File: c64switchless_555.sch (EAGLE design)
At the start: 21 parts, among them IC1 7474N-RP, IC2 NE555, IC3 PIC12F629P, T1 BC547, T2 BC547, X1 B4B-ZR

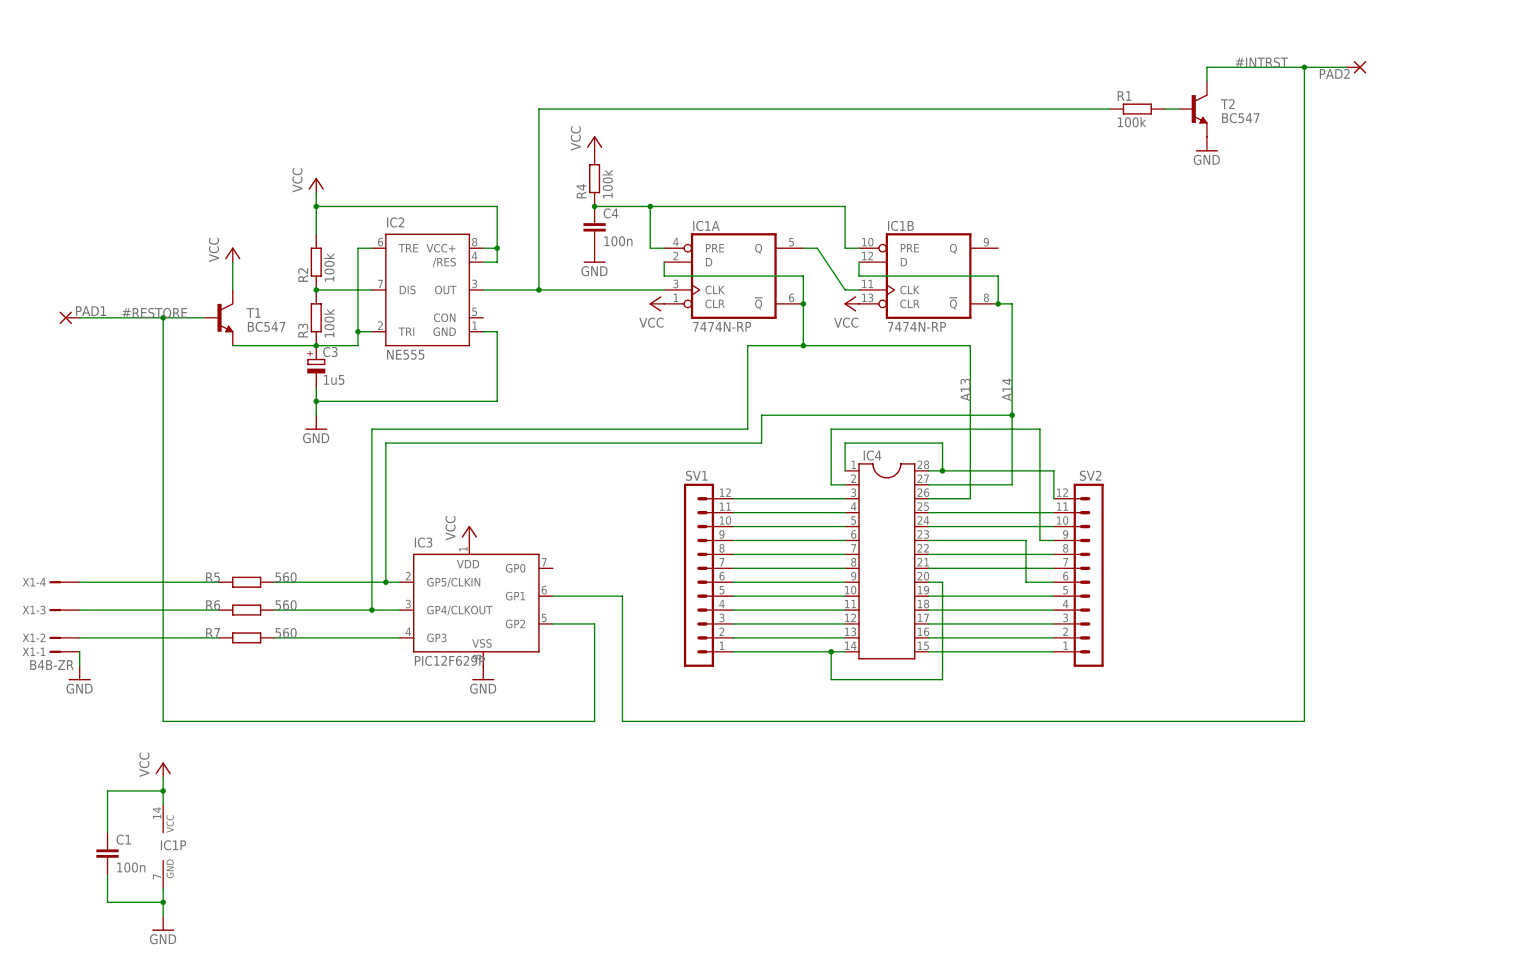
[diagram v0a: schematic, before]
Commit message: PDF file added
Note that this 555 based design is not completed.
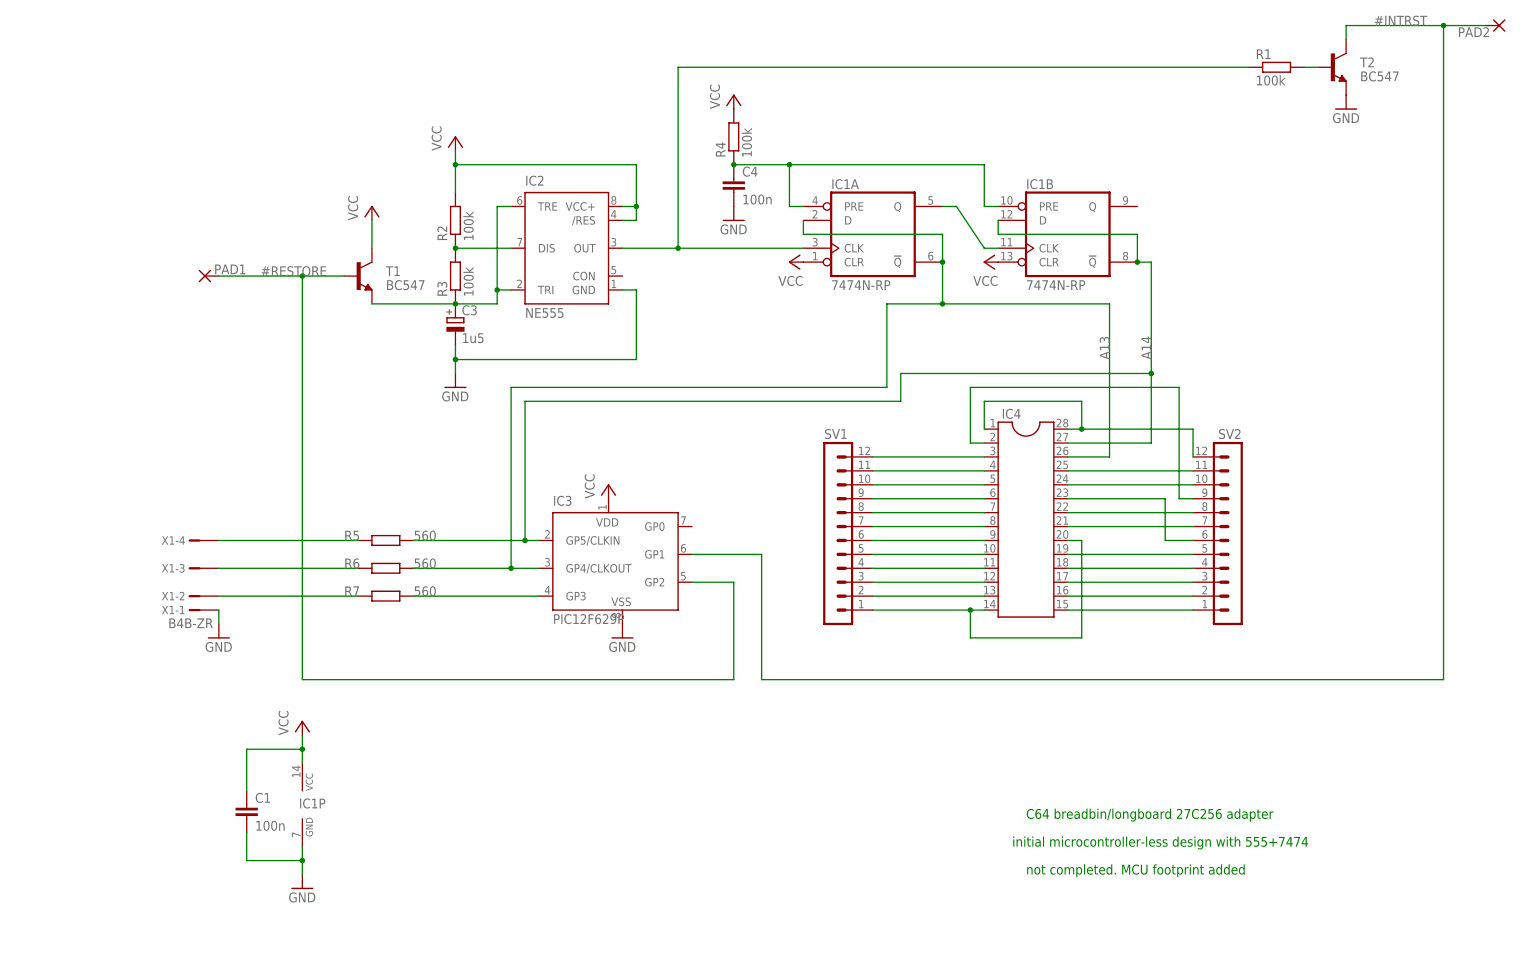
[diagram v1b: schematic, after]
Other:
- note added: "C64 breadbin/longboard 27C256 adapter"
- note added: "initial microcontroller-less design with 555+7474"
- note added: "not completed. MCU footprint added"
- moved on the sheet: C1, C3, C4, IC1A, IC1B, IC1P, IC2, IC3, IC4, PAD1, PAD2, R1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

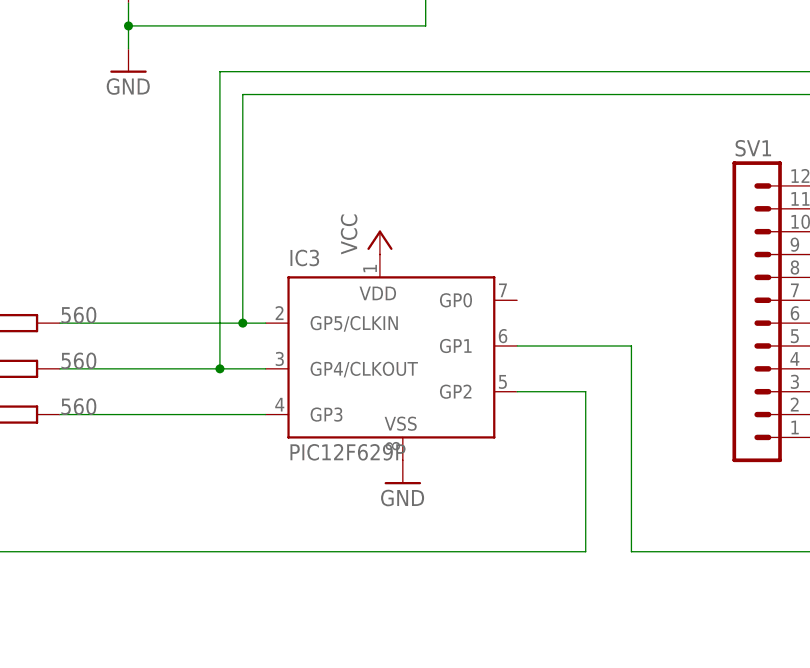
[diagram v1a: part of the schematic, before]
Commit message: Optional MCU
The MCU is optional in the 555 design. I added the footprint because
space was available. Not finished.
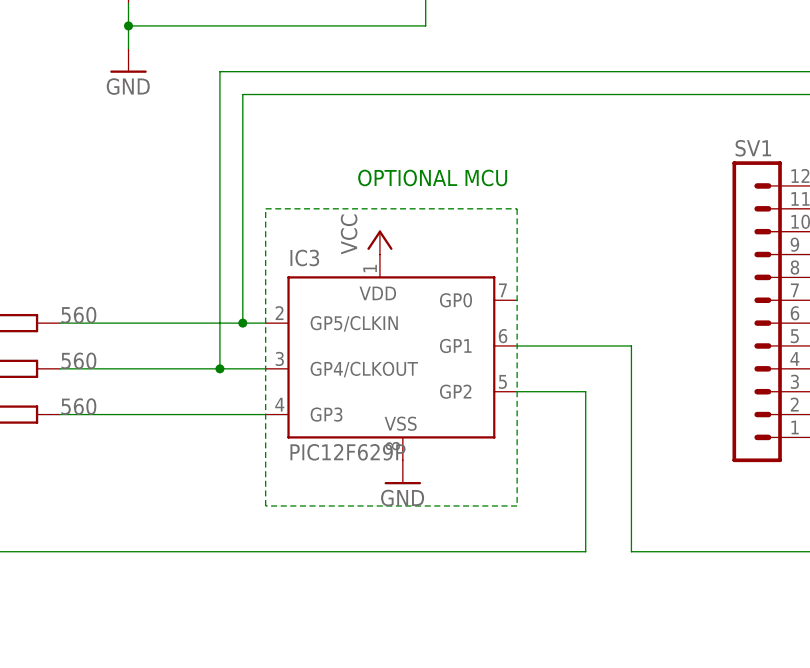
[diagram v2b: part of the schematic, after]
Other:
- note added: "OPTIONAL MCU"
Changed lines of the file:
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@@
 <text x="162.56" y="15.24" size="1.778" layer="91">initial microcontroller-less design with 555+7474</text>
 <text x="165.1" y="10.16" size="1.778" layer="91">not completed. MCU footprint added</text>
+<text x="86.36" y="86.36" size="1.778" layer="91">OPTIONAL MCU</text>
 </plain>
 <instances>
@@
 </segment>
 </net>
+<net name="N$30" class="0">
+<segment>
+<wire x1="76.2" y1="83.82" x2="104.14" y2="83.82" width="0.1524" layer="91" style="longdash"/>
+<wire x1="104.14" y1="83.82" x2="104.14" y2="50.8" width="0.1524" layer="91" style="longdash"/>
+<wire x1="104.14" y1="50.8" x2="76.2" y2="50.8" width="0.1524" layer="91" style="longdash"/>
+<wire x1="76.2" y1="50.8" x2="76.2" y2="83.82" width="0.1524" layer="91" style="longdash"/>
+</segment>
+</net>

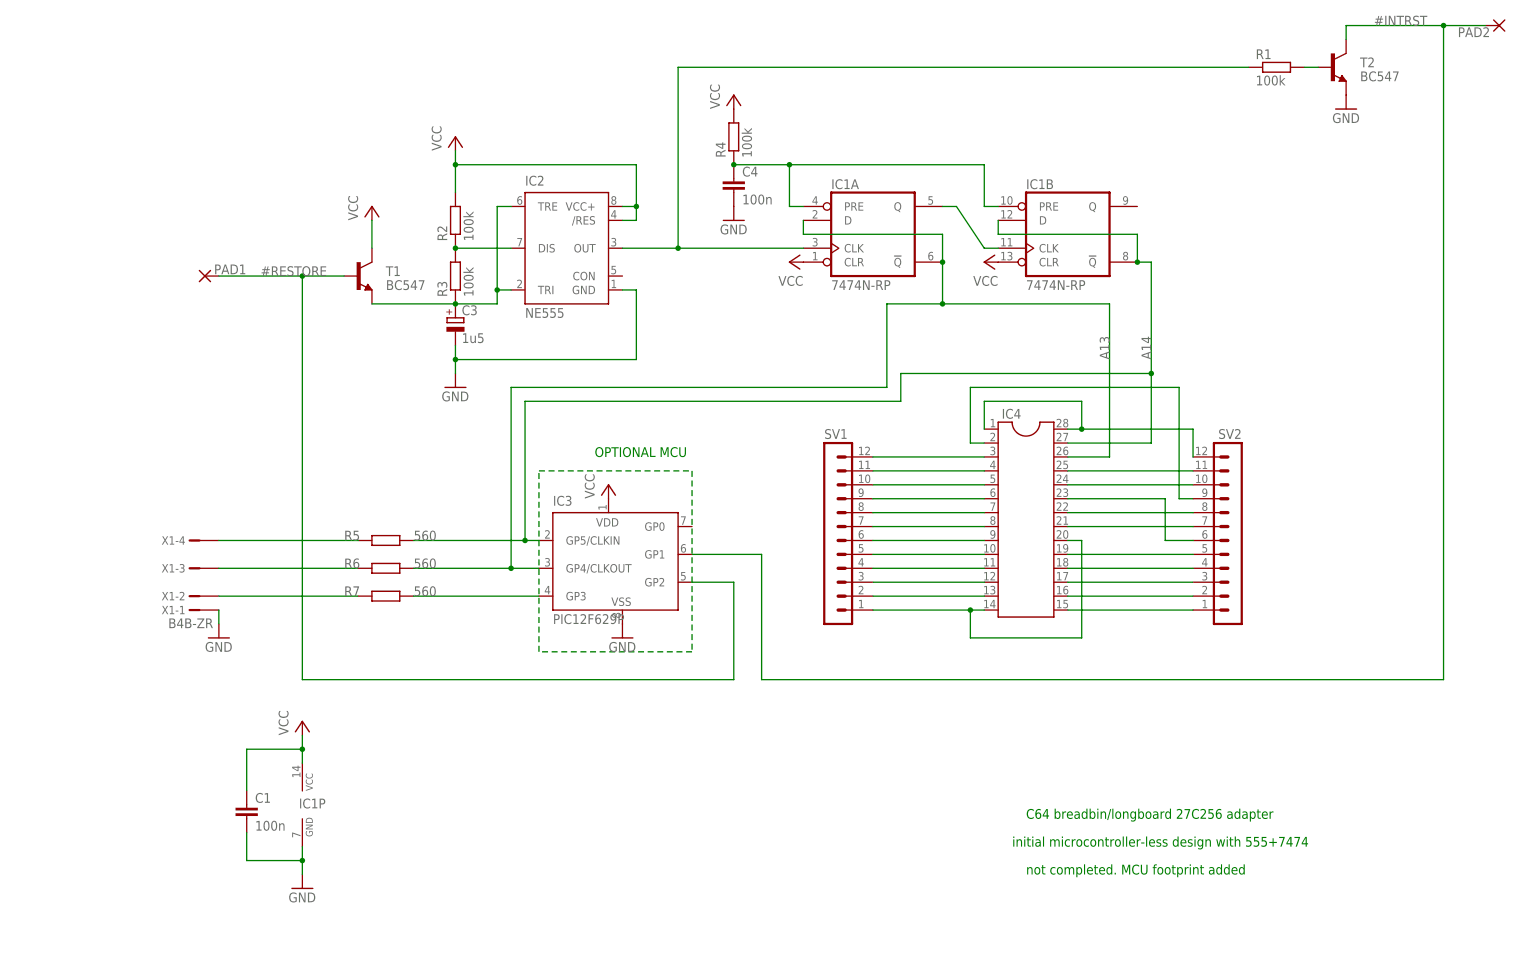
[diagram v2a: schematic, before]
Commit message: 555 based: updated R2,R3. Added revision.
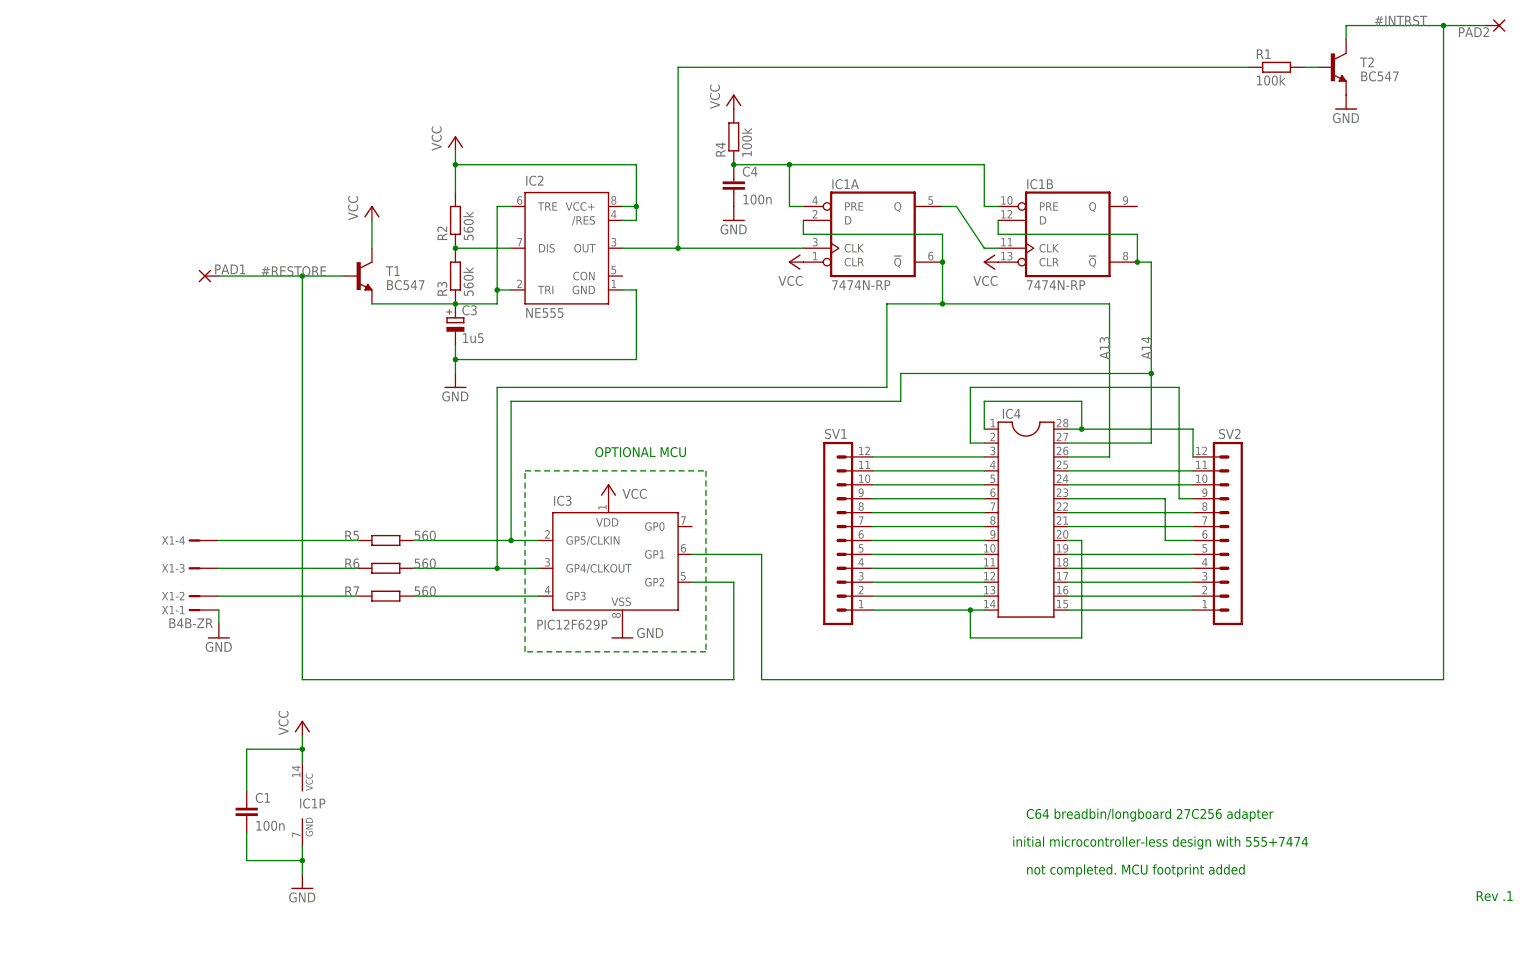
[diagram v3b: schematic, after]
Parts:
- R2, R3: value 100k -> 560k
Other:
- note added: "Rev .1"
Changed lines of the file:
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@@
 <part name="T1" library="transistor" deviceset="BC547" device=""/>
 <part name="P+2" library="supply1" deviceset="VCC" device=""/>
-<part name="R2" library="rcl" deviceset="R-EU_" device="0204/7" value="100k"/>
-<part name="R3" library="rcl" deviceset="R-EU_" device="0204/7" value="100k"/>
+<part name="R2" library="rcl" deviceset="R-EU_" device="0204/7" value="560k"/>
+<part name="R3" library="rcl" deviceset="R-EU_" device="0204/7" value="560k"/>
 <part name="GND3" library="supply1" deviceset="GND" device=""/>
 <part name="P+3" library="supply1" deviceset="VCC" device=""/>
@@
 <text x="165.1" y="10.16" size="1.778" layer="91">not completed. MCU footprint added</text>
 <text x="86.36" y="86.36" size="1.778" layer="91">OPTIONAL MCU</text>
+<text x="247.142" y="5.334" size="1.778" layer="91">Rev .1</text>
 </plain>
 <instances>
 <instance part="IC2" gate="G$1" x="81.28" y="124.46"/>
-<instance part="IC3" gate="G$1" x="88.9" y="66.04"/>
+<instance part="IC3" gate="G$1" x="88.9" y="66.04" smashed="yes">
+<attribute name="NAME" x="78.74" y="77.47" size="1.778" layer="95"/>
+<attribute name="VALUE" x="75.692" y="54.864" size="1.778" layer="96"/>
+</instance>
 <instance part="C1" gate="G$1" x="22.86" y="22.86"/>
 <instance part="C3" gate="G$1" x="60.96" y="111.76"/>
@@
 <instance part="GND4" gate="1" x="111.76" y="129.54"/>
 <instance part="P+6" gate="VCC" x="60.96" y="144.78"/>
-<instance part="P+7" gate="VCC" x="88.9" y="81.28"/>
-<instance part="GND5" gate="1" x="91.44" y="53.34"/>
+<instance part="P+7" gate="VCC" x="88.9" y="81.28" smashed="yes">
+<attribute name="VALUE" x="91.44" y="78.74" size="1.778" layer="96"/>
+</instance>
+<instance part="GND5" gate="1" x="91.44" y="53.34" smashed="yes">
+<attribute name="VALUE" x="93.98" y="53.34" size="1.778" layer="96"/>
+</instance>
 <instance part="X1" gate="-1" x="12.7" y="58.42" rot="R180"/>
 <instance part="X1" gate="-2" x="12.7" y="60.96" rot="R180"/>
@@
 <segment>
 <pinref part="IC3" gate="G$1" pin="GP4/CLKOUT"/>
-<wire x1="76.2" y1="66.04" x2="71.12" y2="66.04" width="0.1524" layer="91"/>
-<wire x1="71.12" y1="66.04" x2="71.12" y2="99.06" width="0.1524" layer="91"/>
-<wire x1="71.12" y1="99.06" x2="139.7" y2="99.06" width="0.1524" layer="91"/>
+<wire x1="76.2" y1="66.04" x2="68.58" y2="66.04" width="0.1524" layer="91"/>
+<wire x1="68.58" y1="66.04" x2="68.58" y2="99.06" width="0.1524" layer="91"/>
+<wire x1="68.58" y1="99.06" x2="139.7" y2="99.06" width="0.1524" layer="91"/>
 <wire x1="139.7" y1="99.06" x2="139.7" y2="114.3" width="0.1524" layer="91"/>
 <pinref part="IC4" gate="G$1" pin="26"/>
@@
 <junction x="149.86" y="114.3"/>
 <pinref part="R6" gate="G$1" pin="2"/>
-<wire x1="53.34" y1="66.04" x2="71.12" y2="66.04" width="0.1524" layer="91"/>
-<junction x="71.12" y="66.04"/>
+<wire x1="53.34" y1="66.04" x2="68.58" y2="66.04" width="0.1524" layer="91"/>
+<junction x="68.58" y="66.04"/>
 </segment>
 </net>
@@
 <label x="187.96" y="104.14" size="1.778" layer="95" rot="R90"/>
 <pinref part="IC3" gate="G$1" pin="GP5/CLKIN"/>
-<wire x1="76.2" y1="71.12" x2="73.66" y2="71.12" width="0.1524" layer="91"/>
-<wire x1="73.66" y1="71.12" x2="73.66" y2="96.52" width="0.1524" layer="91"/>
-<wire x1="73.66" y1="96.52" x2="142.24" y2="96.52" width="0.1524" layer="91"/>
+<wire x1="76.2" y1="71.12" x2="71.12" y2="71.12" width="0.1524" layer="91"/>
+<wire x1="71.12" y1="71.12" x2="71.12" y2="96.52" width="0.1524" layer="91"/>
+<wire x1="71.12" y1="96.52" x2="142.24" y2="96.52" width="0.1524" layer="91"/>
 <wire x1="142.24" y1="96.52" x2="142.24" y2="101.6" width="0.1524" layer="91"/>
 <wire x1="142.24" y1="101.6" x2="187.96" y2="101.6" width="0.1524" layer="91"/>
 <junction x="187.96" y="101.6"/>
 <pinref part="R5" gate="G$1" pin="2"/>
-<wire x1="53.34" y1="71.12" x2="73.66" y2="71.12" width="0.1524" layer="91"/>
-<junction x="73.66" y="71.12"/>
+<wire x1="53.34" y1="71.12" x2="71.12" y2="71.12" width="0.1524" layer="91"/>
+<junction x="71.12" y="71.12"/>
 </segment>
 </net>
@@
 <net name="N$30" class="0">
 <segment>
-<wire x1="76.2" y1="83.82" x2="104.14" y2="83.82" width="0.1524" layer="91" style="longdash"/>
-<wire x1="104.14" y1="83.82" x2="104.14" y2="50.8" width="0.1524" layer="91" style="longdash"/>
-<wire x1="104.14" y1="50.8" x2="76.2" y2="50.8" width="0.1524" layer="91" style="longdash"/>
-<wire x1="76.2" y1="50.8" x2="76.2" y2="83.82" width="0.1524" layer="91" style="longdash"/>
-</segment>
-</net>
+<wire x1="73.66" y1="83.82" x2="106.68" y2="83.82" width="0.1524" layer="91" style="longdash"/>
+<wire x1="106.68" y1="83.82" x2="106.68" y2="50.8" width="0.1524" layer="91" style="longdash"/>
+<wire x1="106.68" y1="50.8" x2="73.66" y2="50.8" width="0.1524" layer="91" style="longdash"/>
+<wire x1="73.66" y1="50.8" x2="73.66" y2="83.82" width="0.1524" layer="91" style="longdash"/>
+</segment>
+</net>
